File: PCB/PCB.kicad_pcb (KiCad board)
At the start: 2 copper layers, 130.8 x 85.1 mm, 44 parts, among them J1 Dynamo, J10 Conn_01x08_Female, J11 Conn_01x01_Female, J12 Conn_01x04_Female, J2 Conn_01x28_Female, J3 Conn_01x02_Female, J4 Conn_01x02_Female, J5 Conn_01x02_Female, J6 Conn_01x02_Female, J7 Conn_01x08_Female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

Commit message: Added PCB images
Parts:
- J1: value Dynamo -> Conn_01x04_Female; footprint TerminalBlock:TerminalBlock_Altech_AK300-2_P5.00mm -> Connector_Molex:Molex_KK-396_A-41791-0004_1x04_P3.96mm_Vertical
- moved J1 2.54 mm to (58.4, 96.5)
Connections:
- J1 pad 2: Net-(D1-Pad1) -> Net-(D2-Pad1)
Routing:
- net Net-(D2-Pad1): track 26.5 -> 36.9 mm
- net Net-(D1-Pad1): track 28.1 -> 33.6 mm

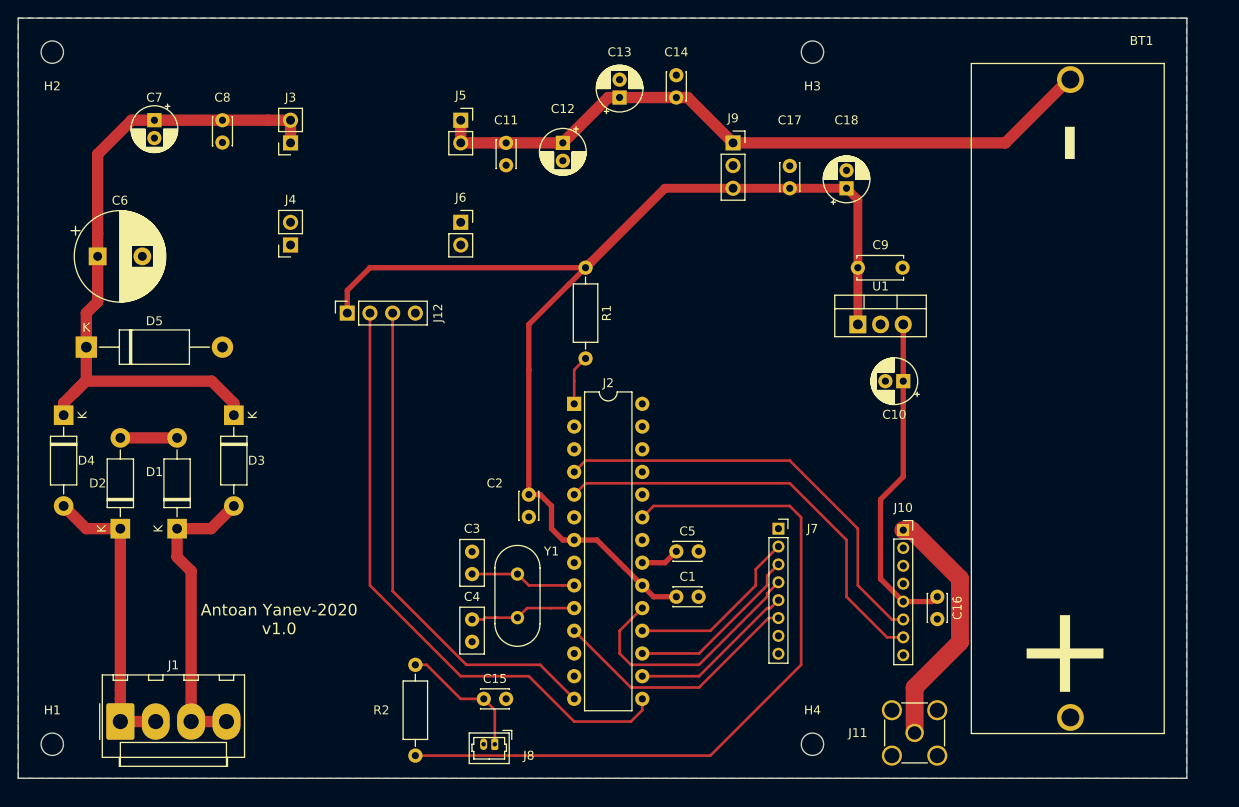
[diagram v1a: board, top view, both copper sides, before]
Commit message: Added GPS control logic
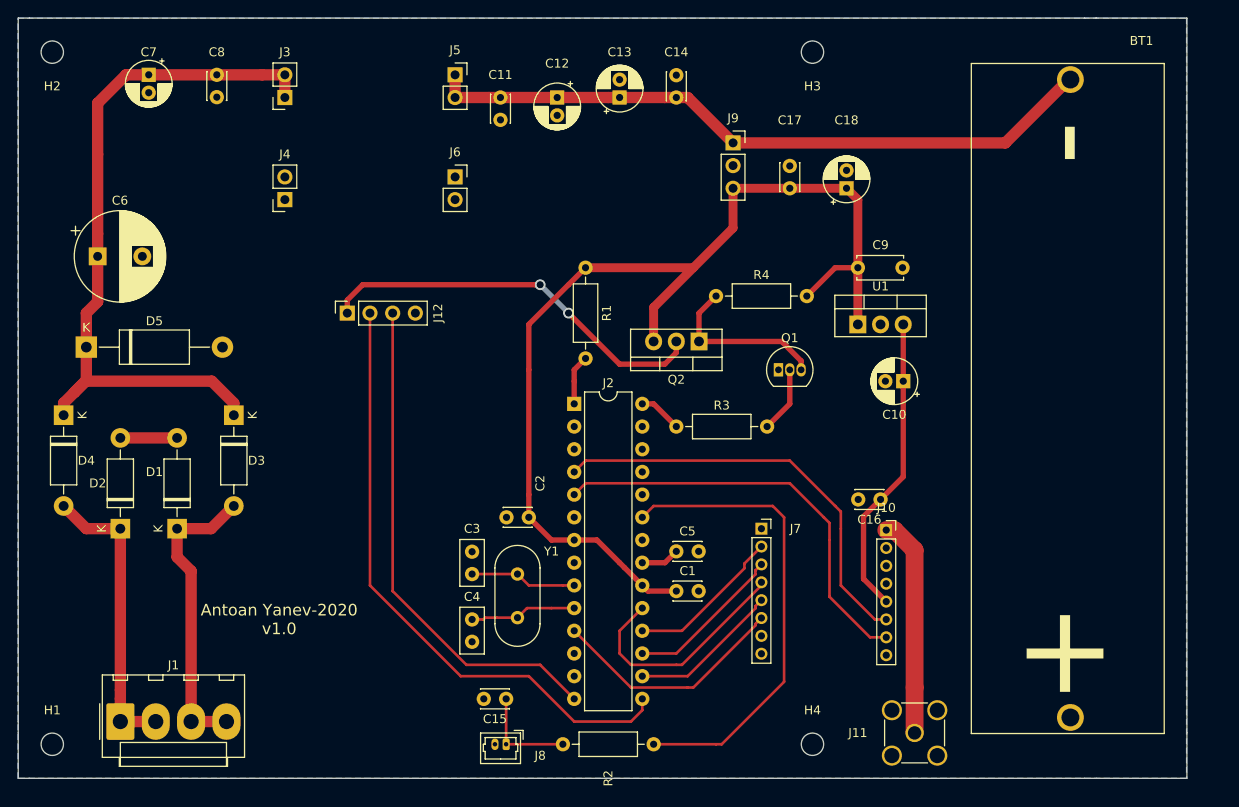
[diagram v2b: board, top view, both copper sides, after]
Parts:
- added Q1: PN2222A, Package_TO_SOT_THT:TO-92_Inline, F.Cu at (132.1, 57.1)
- added Q2: IRF4905, Package_TO_SOT_THT:TO-220-3_Vertical, F.Cu at (123.2, 54.0)
- added R3: 1k, Resistor_THT:R_Axial_DIN0207_L6.3mm_D2.5mm_P10.16mm_Horizontal, F.Cu at (120.7, 63.5)
- added R4: 4.7k, Resistor_THT:R_Axial_DIN0207_L6.3mm_D2.5mm_P10.16mm_Horizontal, F.Cu at (125.1, 48.9)
- moved R2 26.7 mm to (118.1, 99.1), turned to 180 degrees
- moved C16 12.6 mm to (143.5, 71.7), turned to 180 degrees
- moved C7 5.12 mm to (61.6, 24.1)
- moved C8 5.12 mm to (69.2, 24.1)
- moved J5 5.12 mm to (95.9, 24.1)
- moved C12 5.12 mm to (107.3, 26.7)
- moved J3 5.12 mm to (76.8, 26.7)
- moved J4 5.12 mm to (76.8, 38.1)
- moved C11 5.12 mm to (101.0, 26.7)
- moved J6 5.12 mm to (95.9, 35.6)
- moved C2 2.54 mm to (104.1, 73.7), turned to 180 degrees
- moved C15 2.50 mm to (101.6, 94.0), turned to 180 degrees
- moved J10 1.91 mm to (144.1, 75.1)
- moved J7 1.91 mm to (130.2, 74.9)
- moved J8 1.27 mm to (101.6, 99.1)
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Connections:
- J12 pad 1: +5V -> VCCGPS
- J2 pad 28: Net-(J2-Pad28) -> GPSEN
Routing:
- net VCCGPS: track 0.00 -> 44.5 mm, vias 0 -> 2
- net BUTTON: track 82.7 -> 52.8 mm
- net Net-(Q1-Pad3): track 0.00 -> 19.2 mm
- net +5V: track 129.7 -> 118.9 mm
- net Net-(Q1-Pad2): track 0.00 -> 7.40 mm
- net GPSEN: track 0.00 -> 4.86 mm
- net Net-(C6-Pad1): track 77.3 -> 82.1 mm
- net ANT: track 28.0 -> 24.6 mm
- net Net-(C15-Pad1): track 14.8 -> 11.4 mm
- net +3V3: track 37.2 -> 33.9 mm
- net MISO: track 20.2 -> 17.6 mm
- net MOSI: track 20.0 -> 17.7 mm
- net SCK: track 28.5 -> 26.6 mm
- net RESET: track 28.7 -> 26.9 mm
- net NSS: track 18.8 -> 17.0 mm
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
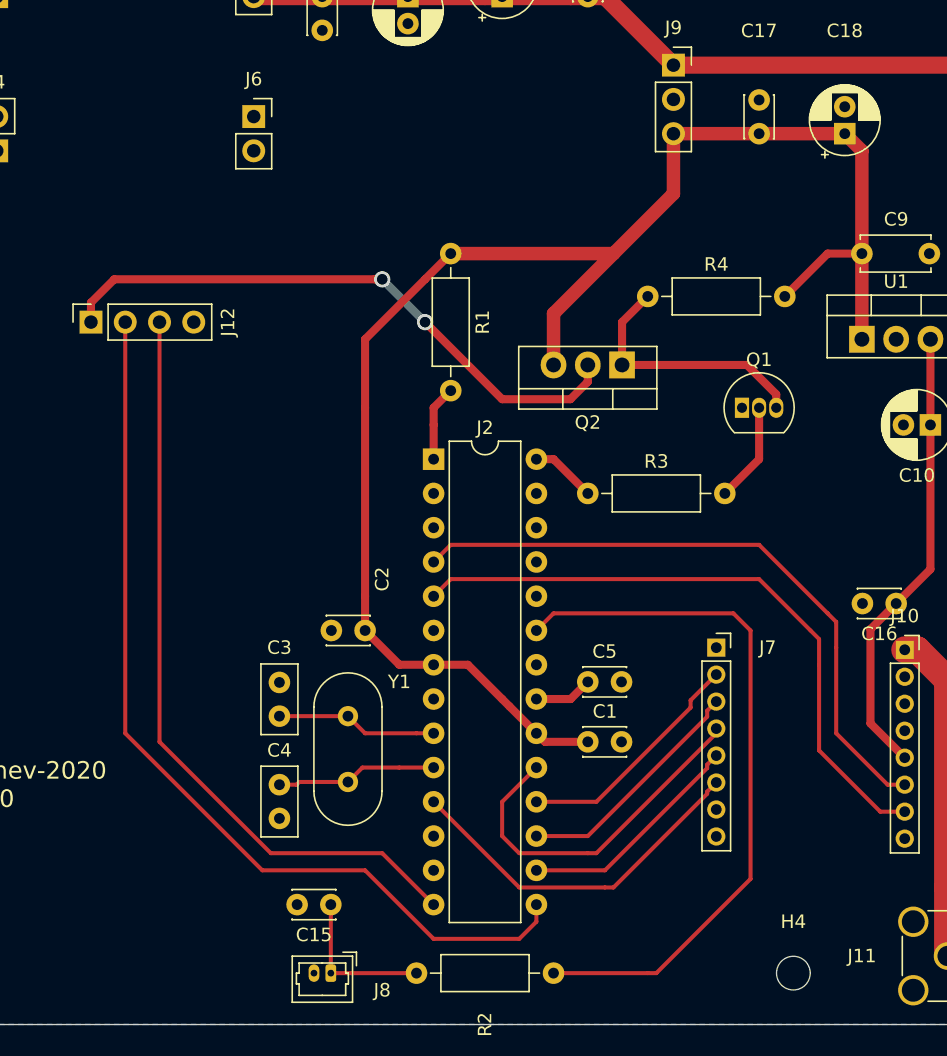
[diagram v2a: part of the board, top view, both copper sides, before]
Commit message: fixed PCB layout and transmitter data fetch bug
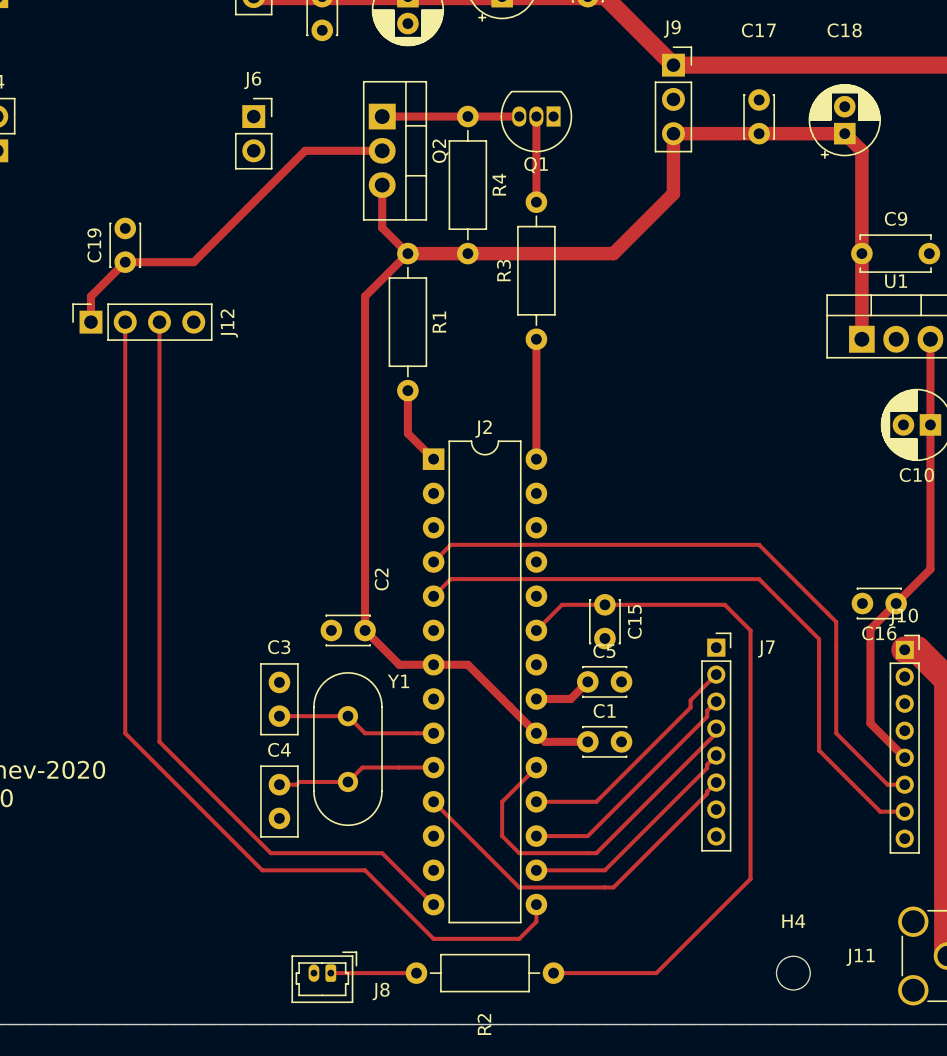
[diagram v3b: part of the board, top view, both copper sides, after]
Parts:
- added C19: 100n, Capacitor_THT:C_Disc_D3.0mm_W2.0mm_P2.50mm, F.Cu at (86.4, 46.4)
- moved C15 30.1 mm to (121.9, 71.8), turned to 270 degrees
- moved Q1 25.7 mm to (118.1, 35.6), turned to 180 degrees
- moved Q2 25.6 mm to (105.4, 35.6), turned to 270 degrees
- moved R4 18.9 mm to (111.8, 35.6), turned to 270 degrees
- moved R3 12.0 mm to (116.8, 52.1), turned to 90 degrees
- moved R1 3.17 mm to (107.3, 45.7)
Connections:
- C15 pad 1: Net-(C15-Pad1) -> BUTTON
- J8 pad 1: Net-(C15-Pad1) -> Net-(J8-Pad1)
- R2 pad 2: Net-(C15-Pad1) -> Net-(J8-Pad1)
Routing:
- net VCCGPS: track 44.5 -> 28.0 mm, vias 2 -> 0
- net Net-(C15-Pad1): track 11.4 -> 0.00 mm
- net +5V: track 118.9 -> 109.5 mm
- net Net-(Q1-Pad3): track 19.2 -> 10.2 mm
- net Net-(J8-Pad1): track 0.00 -> 6.35 mm
- net GPSEN: track 4.86 -> 8.89 mm
- net Net-(Q1-Pad2): track 7.40 -> 6.35 mm
- net BUTTON: track 52.8 -> 53.4 mm

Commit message: Finished Transmitter code and PCB
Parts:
- H1, H2, H3, H4: value MountingHole_2.5mm -> MountingHole_2.5mm_Pad_Via; footprint MountingHole:MountingHole_2.5mm -> MountingHole:MountingHole_2.5mm_Pad_Via
- moved J1 12.1 mm to (70.5, 96.5), turned to 180 degrees
- moved J9 3.18 mm to (130.2, 31.8)
- moved C15 1.91 mm to (121.9, 69.8)
- moved C17 1.91 mm to (135.3, 36.8)
- moved C18 0.64 mm to (140.3, 36.8)
- moved C10 0.63 mm to (146.7, 58.4)
- moved C9 0.63 mm to (141.6, 45.7)
- moved U1 0.63 mm to (141.6, 52.1)
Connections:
- J1 pad 1: Net-(D2-Pad1) -> Net-(D1-Pad1)
- J1 pad 2: Net-(D2-Pad1) -> Net-(D1-Pad1)
- J1 pad 3: Net-(D1-Pad1) -> Net-(D2-Pad1)
- J1 pad 4: Net-(D1-Pad1) -> Net-(D2-Pad1)
- J2 pad 23: BUTTON -> Net-(J2-Pad23)
- J2 pad 5: DIO1 -> BUTTON
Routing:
- net DIO1: track 47.4 -> 0.00 mm
- net BUTTON: track 53.4 -> 61.5 mm
- net +5V: track 109.5 -> 107.5 mm
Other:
- board text added: "Antenna"
- board text added: "Button"
- board text added: "Dynamo"

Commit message: Updated Schematic and PCB
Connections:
- net DIO1 renamed Net-(J10-Pad7)

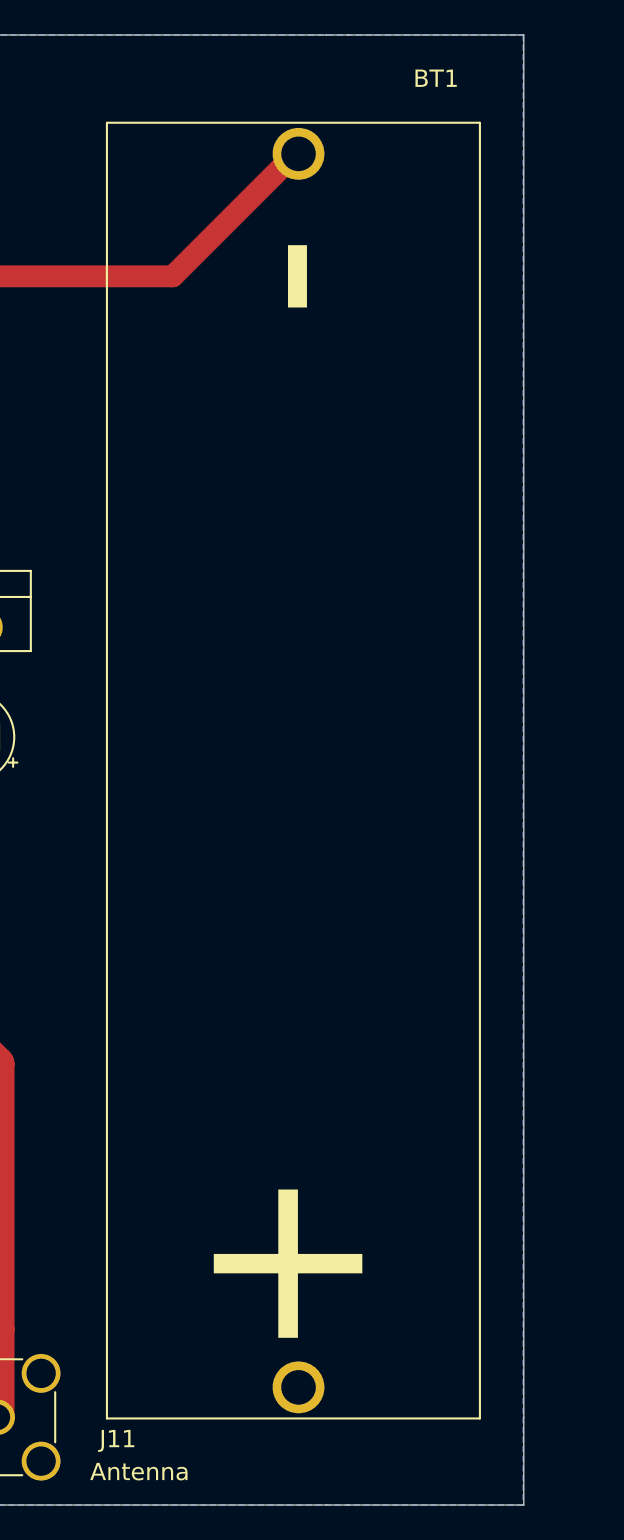
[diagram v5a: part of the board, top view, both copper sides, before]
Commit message: Added Mounting Holes For Battery holder
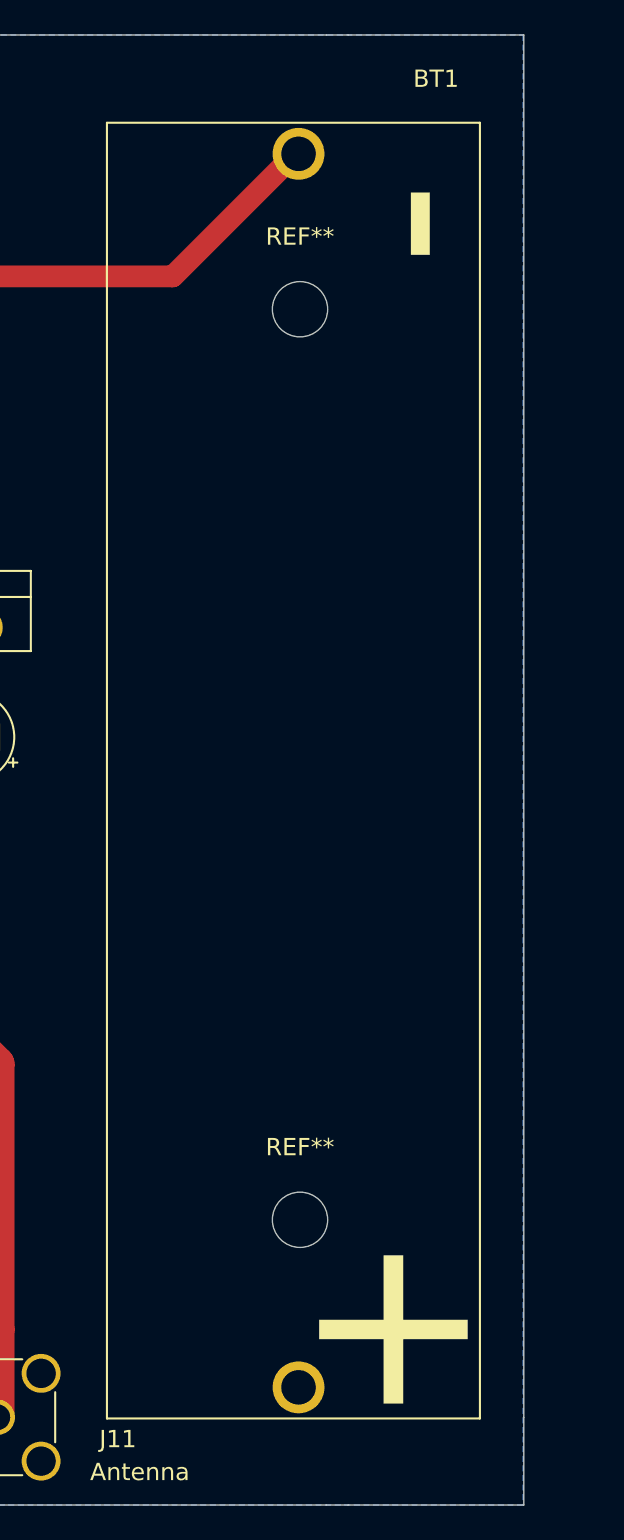
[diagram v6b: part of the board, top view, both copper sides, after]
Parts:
- added REF**: MountingHole_3.2mm_M3, MountingHole:MountingHole_3.2mm_M3, F.Cu at (164.8, 33.7)
- added REF**: MountingHole_3.2mm_M3, MountingHole:MountingHole_3.2mm_M3, F.Cu at (164.8, 86.4)
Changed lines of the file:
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@@
     (tracks 146)
     (zones 0)
-    (modules 49)
+    (modules 51)
     (nets 42)
   )
@@
       (effects (font (size 1 1) (thickness 0.15)))
     )
-    (fp_text user - (at 8.89 11.43 90) (layer F.SilkS)
+    (fp_text user - (at 5.842 4.318 90) (layer F.SilkS)
       (effects (font (size 10 10) (thickness 0.15)))
     )
-    (fp_text user + (at 66.04 11.43 90) (layer F.SilkS)
+    (fp_text user + (at 69.85 5.334 90) (layer F.SilkS)
       (effects (font (size 10 10) (thickness 0.15)))
     )
@@
     )
   )
+  (module MountingHole:MountingHole_3.2mm_M3 (layer F.Cu)
+    (at 164.846 33.655)
+    (descr "Mounting Hole 3.2mm, no annular, M3")
+    (tags "mounting hole 3.2mm no annular m3")
+    (attr virtual)
+    (fp_text reference REF** (at 0 -4.2) (layer F.SilkS)
+      (effects (font (size 1 1) (thickness 0.15)))
+    )
+    (fp_text value MountingHole_3.2mm_M3 (at 0 4.2) (layer F.Fab)
+      (effects (font (size 1 1) (thickness 0.15)))
+    )
+    (fp_circle (center 0 0) (end 3.45 0) (layer F.CrtYd) (width 0.05))
+    (fp_circle (center 0 0) (end 3.2 0) (layer Cmts.User) (width 0.15))
+    (fp_text user %R (at 0.3 0) (layer F.Fab)
+      (effects (font (size 1 1) (thickness 0.15)))
+    )
+    (pad 1 np_thru_hole circle (at 0 0) (size 3.2 3.2) (drill 3.2) (layers *.Cu *.Mask))
+  )
+  (module MountingHole:MountingHole_3.2mm_M3 (layer F.Cu)
+    (at 164.846 86.36)
+    (descr "Mounting Hole 3.2mm, no annular, M3")
+    (tags "mounting hole 3.2mm no annular m3")
+    (attr virtual)
+    (fp_text reference REF** (at 0 -4.2) (layer F.SilkS)
+      (effects (font (size 1 1) (thickness 0.15)))
+    )
+    (fp_text value MountingHole_3.2mm_M3 (at 0 4.2) (layer F.Fab)
+      (effects (font (size 1 1) (thickness 0.15)))
+    )
+    (fp_circle (center 0 0) (end 3.45 0) (layer F.CrtYd) (width 0.05))
+    (fp_circle (center 0 0) (end 3.2 0) (layer Cmts.User) (width 0.15))
+    (fp_text user %R (at 0.3 0) (layer F.Fab)
+      (effects (font (size 1 1) (thickness 0.15)))
+    )
+    (pad 1 np_thru_hole circle (at 0 0) (size 3.2 3.2) (drill 3.2) (layers *.Cu *.Mask))
+  )
   (gr_text Antenna (at 155.575 100.965) (layer F.SilkS)

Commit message: Rotated LoRa Module
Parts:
- removed REF** (x2): MountingHole_3.2mm_M3, MountingHole:MountingHole_3.2mm_M3
- moved J7 17.3 mm to (147.5, 75.9), turned to 270 degrees
- moved C16 15.2 mm to (150.6, 85.1), turned to 270 degrees
- moved J10 15.2 mm to (147.3, 89.9), turned to 270 degrees
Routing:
- net BUTTON: track 61.5 -> 89.7 mm
- net MISO: track 17.6 -> 42.0 mm
- net DIO0: track 47.7 -> 71.1 mm
- net MOSI: track 17.7 -> 40.3 mm
- net SCK: track 26.6 -> 48.1 mm
- net NSS: track 17.0 -> 36.8 mm
- net ANT: track 24.6 -> 7.88 mm
- net +3V3: track 34.2 -> 50.3 mm
- net RESET: track 26.9 -> 40.2 mm
